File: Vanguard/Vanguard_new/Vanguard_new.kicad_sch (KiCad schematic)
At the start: 40 parts, among them J1 USB_B_Micro, J2 Conn_02x03_Pin, Q1 BSS138, Q2 BSS138, Q3 BSS138, U1 ATSAMD11D14A-M, U2 ATmega4809-A, U3 BD1020HFV, U4 AP2112K-3.3, U5 MPM3610AGQV-P, U6 BNO086

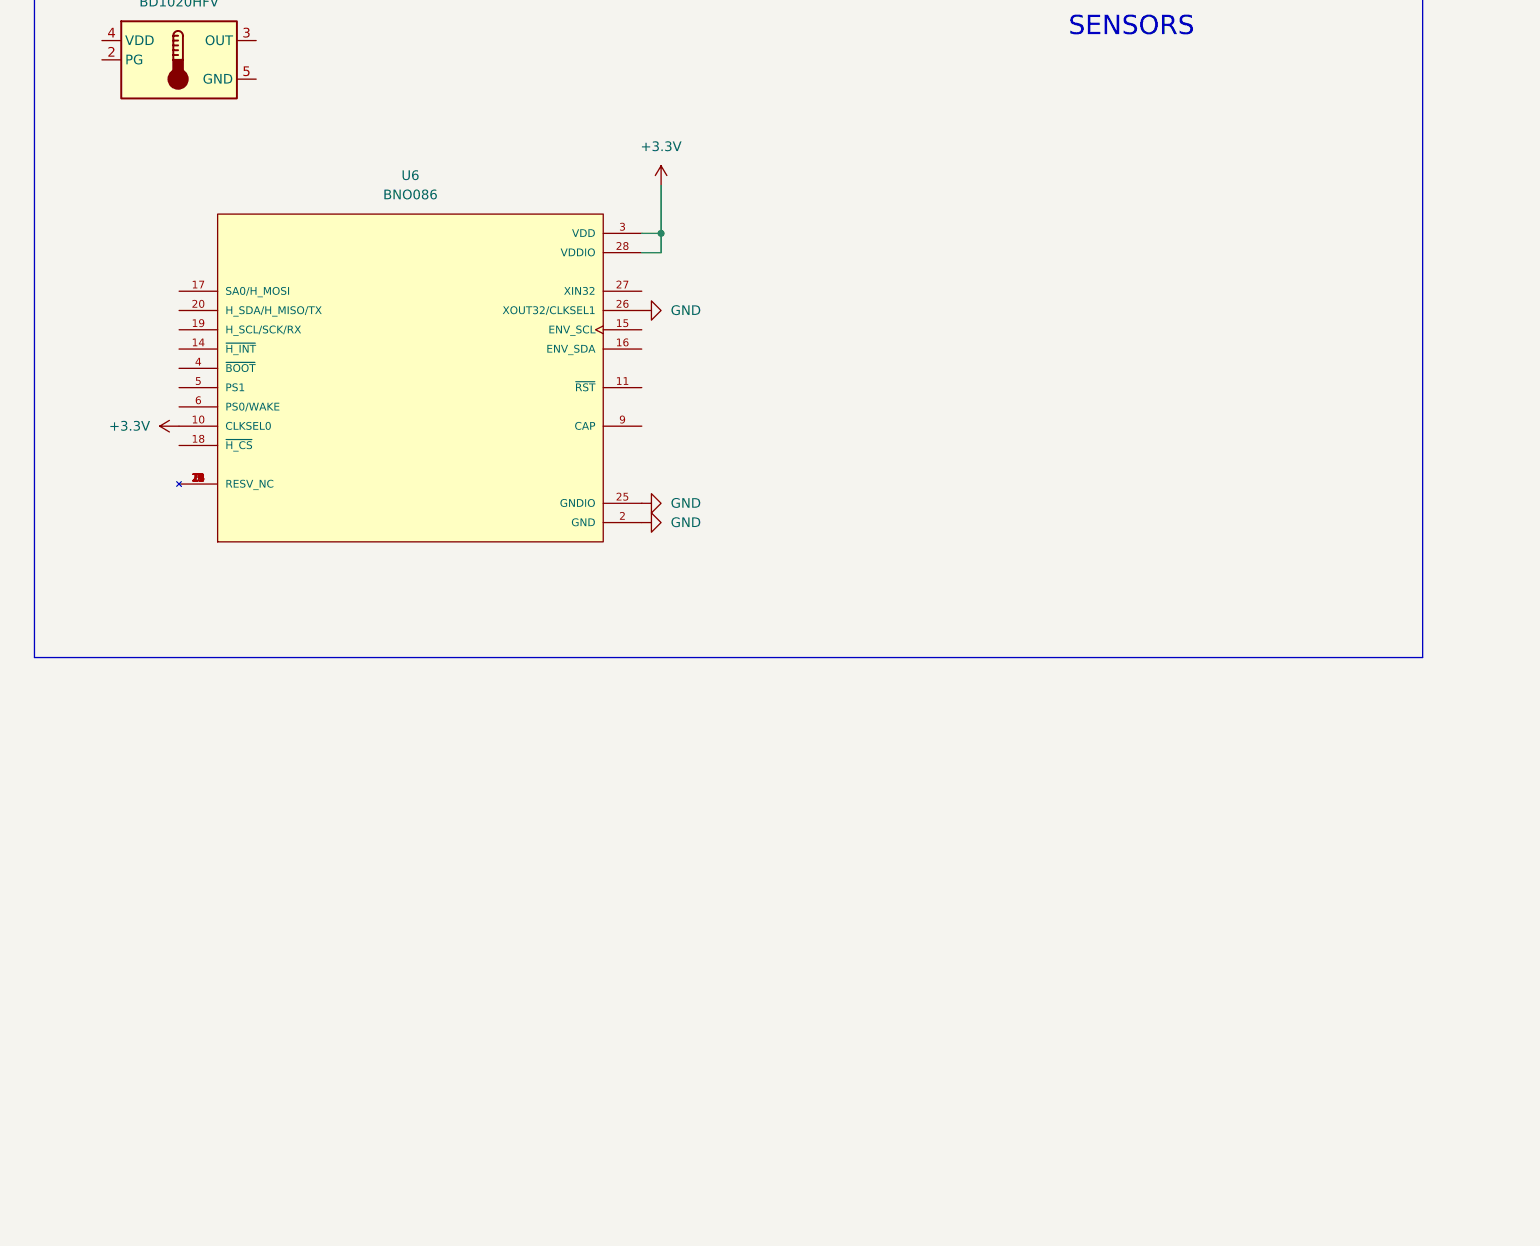
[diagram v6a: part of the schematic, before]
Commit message: finished bno086
based off of https://docs.sparkfun.com/SparkFun_VR_IMU_Breakout_BNO086_QWIIC/assets/board_files/SparkFun_VR_IMU_Breakout_BNO086_QWIIC_Schematic_v10.pdf
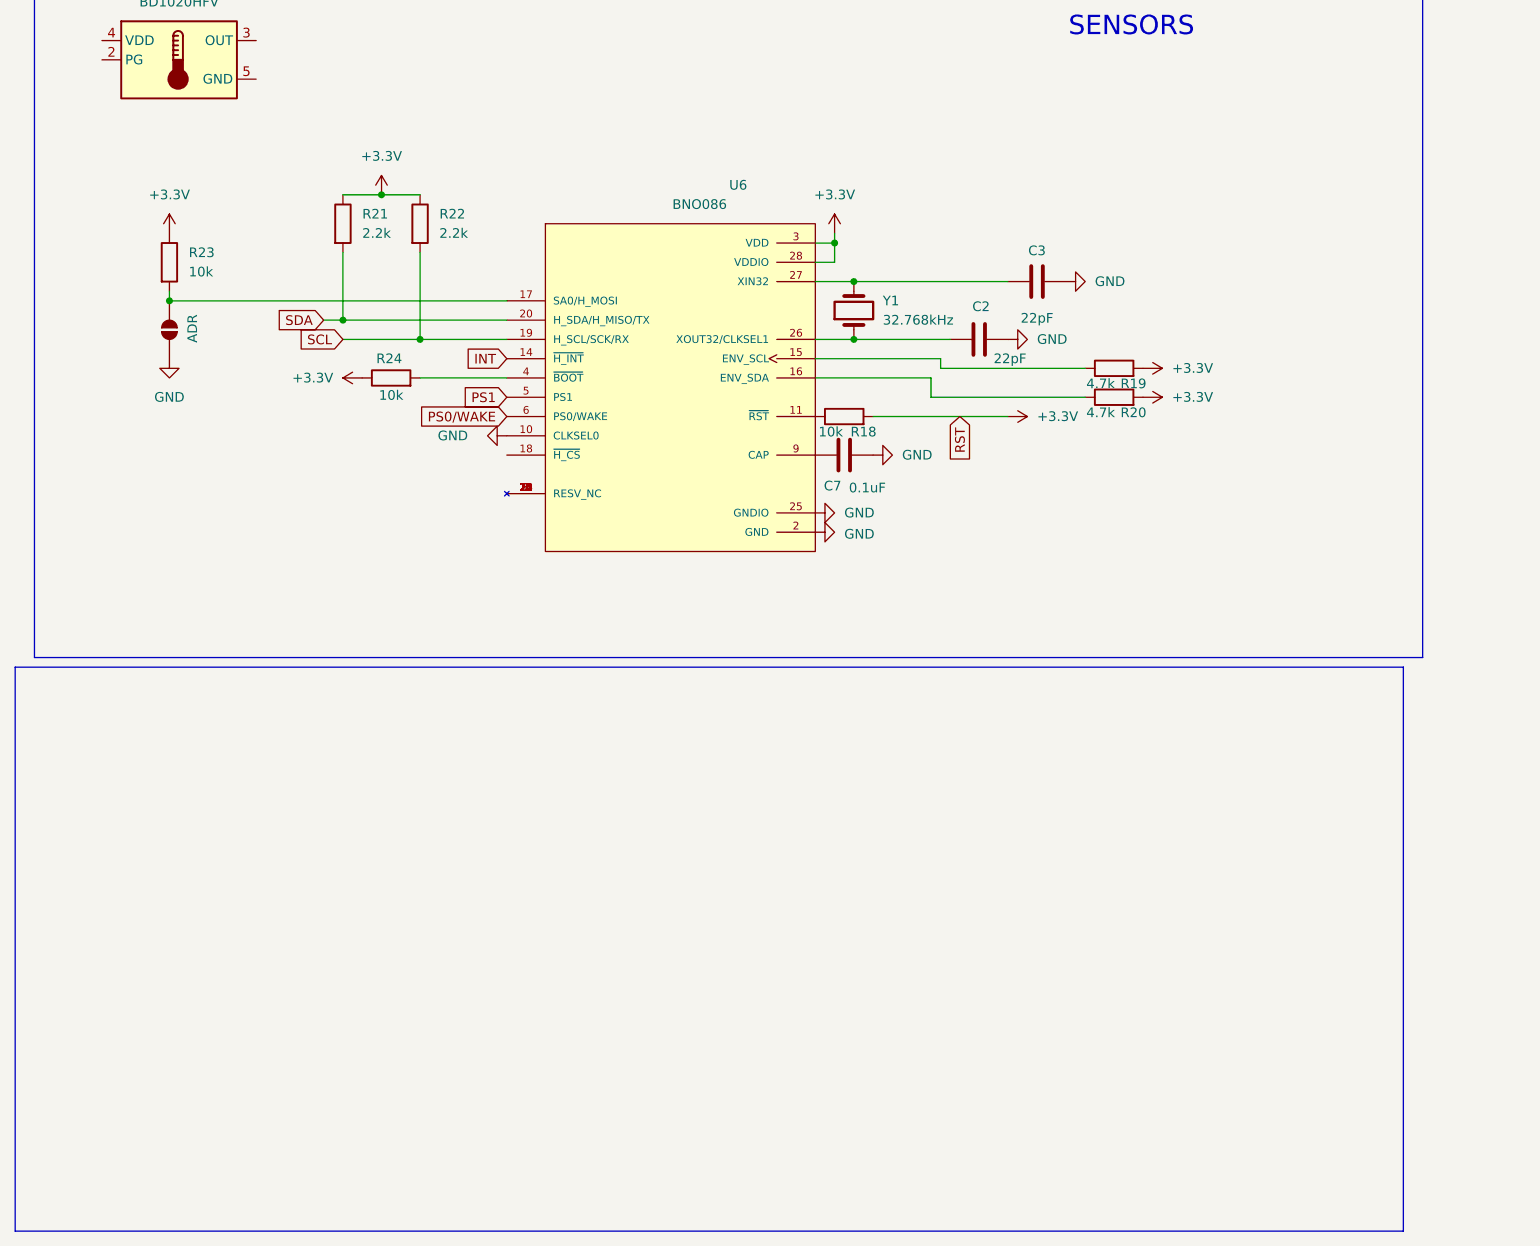
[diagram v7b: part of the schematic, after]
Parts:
- added ADR: ~, symbol Jumper:SolderJumper_2_Open
- added C2, C3: 22pF, symbol Device:C
- added C7: 0.1uF, symbol Device:C
- added R18, R23, R24: 10k, symbol Device:R
- added R19, R20: 4.7k, symbol Device:R
- added R21, R22: 2.2k, symbol Device:R
- added Y1: 32.768kHz, symbol Device:Crystal
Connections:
- net +3.3V: now also R18.2, R19.2, R20.2, R21.1, R22.1, R23.1, R24.1; no longer U6.10 (CLKSEL0)
- net GND: now also U6.10 (CLKSEL0), ADR.1 (A), C2.2, C3.2, C7.2; no longer U6.26 (XOUT32/CLKSEL1)
- net at U6.11 (~{RST}): now also R18.1
- net INT: now reaches U6.14 (~{H_INT})
- net at U6.15 (ENV_SCL): now also R19.1
- net at U6.16 (ENV_SDA): now also R20.1
- net at U6.17 (SA0/H_MOSI): now also ADR.2 (B), R23.2
- net SCL: now reaches U6.19 (H_SCL/SCK/RX)
- net SCL: now also R22.2
- net SDA: now reaches U6.20 (H_SDA/H_MISO/TX)
- net SDA: now also R21.2
- net at U6.27 (XIN32): now also C3.1, Y1.2
- net at U6.4 (~{BOOT}): now also R24.2
- net PS1: now reaches U6.5 (PS1)
- net PS0/WAKE: now reaches U6.6 (PS0/WAKE)
- net at U6.9 (CAP): now also C7.1
- new net: C2.1, U6.26 (XOUT32/CLKSEL1), Y1.1
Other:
- moved on the sheet: U6

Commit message: sd card done
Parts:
- added J3: Micro_SD_Card_Det1, symbol Connector:Micro_SD_Card_Det1
- added U7: TXB0104D, Package_SO:SOIC-14_3.9x8.7mm_P1.27mm, symbol Logic_LevelTranslator:TXB0104D
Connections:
- net +3.3V: now also J3.6 (VSS), U7.1 (VCCA), U7.14 (VCCB), U7.8 (OE)
- net GND: now also J3.10 (SHIELD), J3.4 (VDD), U7.7 (GND)
- net D5: now reaches U2.22 (PD2)
- net D5: now also U7.10 (B4)
- net D4: now reaches U2.23 (PD3)
- net D4: now also U7.11 (B3)
- net D6: now reaches U2.24 (PD4)
- net D6: now also U7.12 (B2)
- net D7: now reaches U2.25 (PD5)
- net D7: now also U7.13 (B1)
- net CD: now reaches U2.26 (PD6)
- net CD: now also J3.9 (DET)
- new net: J3.8 (DAT1), U7.2 (A1)
- new net: J3.7 (DAT0), U7.3 (A2)
- new net: J3.5 (CLK), U7.4 (A3)
- new net: J3.3 (CMD), U7.5 (A4)
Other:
- note added: "SD CARD"
